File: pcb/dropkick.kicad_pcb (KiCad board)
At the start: 2 copper layers, 44.5 x 50.8 mm, 51 parts, among them SW1 CONN3_020524_WRE, SW2 KMR211NG_LFS, U1 ATSAMD21G18A-AUT, U2 SAM-M8Q-0-10, U3 MCP73831T-2ACI/OT, U4 DPS310, U5 MPU-6050, U6 SPX3819-3.3, X1 microUSB, X2 JSTPH, X3 microsd, X5 32768Hz

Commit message: V2-SAM working draft
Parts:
- removed the C5 at (77.7, 85.9)
- removed JP2: 20021221-00010C4LF, lib_fr:3221-10-0300-00-TR
- removed JP4: HEADER-1X12, lib_fr:1X12_ROUND
- removed JP5: HEADER-1X16ROUND, lib_fr:1X16_ROUND
- removed R11: 4.7K, lib_fr:RESPACK_4X0603
- removed R14: 10K, lib_fr:0603-NO
- removed SJ4: SOLDERJUMPER, lib_fr:0603-NO
- removed TP1: TESTPOINTROUND1.5MM, lib_fr:TESTPOINT_ROUND_1.5MM
- removed X5: 32768Hz, lib_fr:XTAL3215
- added J1: Conn_01x08, Connector_PinHeader_2.54mm:PinHeader_1x09_P2.54mm_Vertical, F.Cu at (105.7, 55.0)
- added JP1: 3221-10-0300-00-TR, lib_fr:3221-10-0300-00-TR, B.Cu at (97.7, 55.7)
- added R4: 10K, Resistor_SMD:R_0603_1608Metric, F.Cu at (79.6, 57.7)
- added R5: 1K, Resistor_SMD:R_0603_1608Metric, F.Cu at (82.9, 50.2)
- added REF2: OSHW-Logo2_7.3x6mm_SilkScreen, Symbol:OSHW-Logo2_7.3x6mm_SilkScreen, F.Cu at (70.5, 86.7)
- added X4: 32768Hz, lib_fr:XTAL3215, F.Cu at (83.7, 61.6)
- C1: footprint lib_fr:0603-NO -> Capacitor_SMD:C_0603_1608Metric
- C10: renamed from C11; value 10uF -> 0.1uF; footprint lib_fr:0805-NO -> Capacitor_SMD:C_0603_1608Metric
- C2, C3, C4: footprint lib_fr:0805-NO -> Capacitor_SMD:C_0805_2012Metric
- C5: renamed from C6; value 0.1uF -> 10uF; footprint lib_fr:0603-NO -> Capacitor_SMD:C_0805_2012Metric
- C6: renamed from C7; footprint lib_fr:0603-NO -> Capacitor_SMD:C_0603_1608Metric
- C7: renamed from C8; footprint lib_fr:0603-NO -> Capacitor_SMD:C_0603_1608Metric
- C8: renamed from C9; footprint lib_fr:0805-NO -> Capacitor_SMD:C_0805_2012Metric
- C9: renamed from C10; footprint lib_fr:0603-NO -> Capacitor_SMD:C_0603_1608Metric
- CHG1, L1, L2: footprint lib_fr:CHIPLED_0805_NOOUTLINE -> lib_fr:CHIPLED_0603_NOOUTLINE
- D1: moved to B.Cu
- R10, R7: footprint lib_fr:0603-NO -> Resistor_SMD:R_0603_1608Metric
- R2: value 100K -> 100k
- R3: value 100k -> 100K
- R6: value 10K -> 2.2K; footprint lib_fr:0603-NO -> Resistor_SMD:R_0603_1608Metric
- R8: value 2.2K -> 10K; footprint lib_fr:0603-NO -> Resistor_SMD:R_0603_1608Metric
- R9: value 1K -> 10K; footprint lib_fr:0603-NO -> Resistor_SMD:R_0603_1608Metric
- SW1: value CONN3_020524_WRE -> 450405020524
- U1: value ATSAMD21G18A-AUT -> SPX3819-3.3; footprint lib_fr:ATSAMD21G15B-AU -> lib_fr:SOT23-5
- U4: value DPS310 -> ATSAMD21G18A-AUT; footprint lib_fr:DPS310XTSA1 -> lib_fr:ATSAMD21G15B-AU
- U5: value MPU-6050 -> DPS310XTSA1; footprint lib_fr:QFN24_4MM_SMSC -> lib_fr:DPS310XTSA1
- U6: value SPX3819-3.3 -> MPU-6050; footprint lib_fr:SOT23-5 -> lib_fr:QFN24_4MM_SMSC
- moved D2 46.0 mm to (74.2, 45.7), turned to -90 degrees
- moved R10 43.2 mm to (102.9, 58.8), turned to -90 degrees
- moved C10 30.2 mm to (96.9, 66.3), turned to -90 degrees
- moved C12 27.1 mm to (101.7, 64.3), turned to 90 degrees
- moved R8 27.0 mm to (72.6, 48.2), turned to 0 degrees
- moved C11 26.1 mm to (101.4, 72.8), turned to 0 degrees
- moved D1 24.7 mm to (79.3, 50.5), turned to 180 degrees
- moved C5 24.5 mm to (75.5, 84.0), turned to 180 degrees
- moved R3 24.4 mm to (82.5, 69.4), turned to -90 degrees
- moved R9 24.2 mm to (101.0, 58.8)
- moved C2 23.1 mm to (85.6, 54.8)
- moved U5 22.9 mm to (99.2, 63.0)
- moved U4 20.0 mm to (90.2, 65.3), turned to 0 degrees
- moved R2 18.8 mm to (94.6, 53.5)
- moved R6 16.3 mm to (98.7, 46.9)
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- renumbered C12 to C11, C13 to C12, REF** to REF1
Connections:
- C10 pad 1: 3.3V -> +3V3
- C5 pad 1: 3.3V -> +3V3
- C6 pad 1: Net-(C7-Pad1) -> Net-(C6-Pad1)
- C7 pad 1: Net-(C8-Pad1) -> Net-(C7-Pad1)
- C9 pad 1: Net-(C10-Pad1) -> Net-(C9-Pad1)
- R10 pad 1: 3.3V -> +3V3
- R10 pad 2: Net-(D2-PadA) -> /SDA
- R2 pad 1: /D9 -> VBUS
- R2 pad 2: GND -> /EN
- R3 pad 1: VBUS -> /D9
- R3 pad 2: /EN -> GND
- R6 pad 1: Net-(R6-Pad1) -> /D13
- R6 pad 2: GND -> Net-(L2-PadA)
- R7 pad 1: Net-(CHG1-PadC) -> Net-(L1-PadC)
- R7 pad 2: Net-(R7-Pad2) -> GND
- R8 pad 1: /D13 -> +3V3
- R8 pad 2: Net-(L2-PadA) -> Net-(D2-PadA)
- R9 pad 1: Net-(L1-PadC) -> +3V3
- R9 pad 2: GND -> /SCL
- U1 pad 1: Net-(C7-Pad1) -> VBUS
- U1 pad 2: Net-(C8-Pad1) -> GND
- U1 pad 3: /A0 -> /EN
- U1 pad 4: /AREF -> unconnected-(U1-Pad4)
- U1 pad 5: GND -> +3V3
- U2 pad 17: 3.3V -> +3V3
- U2 pad 2: 3.3V -> +3V3
- U3 pad 1: Net-(R7-Pad2) -> Net-(R5-Pad2)
- U3 pad 5: Net-(R6-Pad1) -> Net-(R4-Pad1)
- U4 pad 1: GND -> Net-(C6-Pad1)
- U4 pad 2: GND -> Net-(C7-Pad1)
- U4 pad 3: /SDA -> /A0
- U4 pad 4: /SCL -> /AREF
- U4 pad 6: 3.3V -> +3V3
- U4 pad 7: GND -> /A1
- U4 pad 8: 3.3V -> /A2
- U5 pad 2: (no net) -> GND
- U5 pad 3: (no net) -> /SDA
- U5 pad 4: (no net) -> /SCL
- U5 pad 5: (no net) -> GND
- U5 pad 6: /SDA_EXT -> +3V3
- U5 pad 7: /SCL_EXT -> GND
- U5 pad 8: 3.3V -> +3V3
- U6 pad 1: VBUS -> GND
- U6 pad 2: GND -> (no net)
- U6 pad 3: /EN -> (no net)
- U6 pad 4: unconnected-(U6-Pad4) -> (no net)
- U6 pad 5: +3V3 -> (no net)
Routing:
- net GND: track 337.6 -> 75.3 mm, vias 1 -> 18
- net 3.3V: track 116.2 -> 0.00 mm, vias 3 -> 0
- net +3V3: track 118.3 -> 230.0 mm
- net /SCL: track 109.6 -> 40.3 mm, vias 2 -> 3
- net /SDA: track 105.4 -> 51.7 mm
- net VCC: track 37.4 -> 0.00 mm, vias 1 -> 0
- net /D8: track 58.3 -> 27.0 mm, vias 6 -> 0
- net /A5: track 30.9 -> 0.00 mm, vias 1 -> 0
- net /MOSI: track 55.6 -> 26.0 mm
- net /D7: track 50.3 -> 22.0 mm
- net /~{RESET}: track 46.6 -> 18.6 mm, vias 1 -> 0
- net VBUS: track 65.1 -> 37.1 mm, vias 2 -> 3
- net /A1: track 25.4 -> 0.00 mm
- net /A2: track 24.5 -> 0.00 mm
- net /A4: track 24.0 -> 0.00 mm
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- added copper zone on In1.Cu, net GND
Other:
- outline, holes or cut-outs redrawn
- copper layers 2 -> 4
- board text added: "+3.3"
- board text added: "A0"
- board text added: "AREF"
- board text added: "D0"
- board text added: "D1"
- board text added: "Dropkick V2-SAM Copyright (c) 2022 Riley Rainey https://GitHub.com/rrainey/dropkick/"
- board text added: "Dropkick V2-SAM Riley Rainey"
- board text added: "GND"
- board text added: "SCL"
- board text added: "SDA"
- board text added: "VBAT"
- board text removed: "Dropkick V1 Copyright (c) 2022 Riley Rainey https://GitHub.com/rrainey/dropkick/"

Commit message: test of 4-layer PCB
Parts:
- D1: moved to F.Cu
- moved C3 16.8 mm to (80.0, 54.2)
- moved C8 8.26 mm to (73.0, 54.4), turned to 90 degrees
- moved R5 7.65 mm to (75.3, 50.6), turned to -90 degrees
- moved D1 7.48 mm to (77.3, 57.7)
- moved R4 6.56 mm to (78.0, 51.3)
- moved U3 4.22 mm to (76.6, 54.1), turned to -90 degrees
- moved C4 2.04 mm to (97.5, 55.9)
- moved U1 2.04 mm to (93.8, 54.3)
- moved R2 2.04 mm to (96.6, 53.1)
- moved C2 0.95 mm to (86.5, 54.7), turned to 90 degrees
- moved R8 0.70 mm to (72.6, 47.5)
- moved C10 0.69 mm to (97.5, 66.7)
- moved C12 0.19 mm to (101.9, 64.3)
- moved C11 0.19 mm to (101.6, 72.7)
- moved U5 0.19 mm to (99.4, 63.0)
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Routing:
- net +3V3: track 230.0 -> 190.2 mm, vias 6 -> 5
- net /D+: track 44.3 -> 17.1 mm, vias 2 -> 0
- net /D-: track 38.1 -> 17.8 mm
- net /D13: track 35.1 -> 22.3 mm, vias 2 -> 0
- net /SCK: track 31.7 -> 22.8 mm, vias 2 -> 1
- net /SCL: track 40.3 -> 47.9 mm
- net VBUS: track 37.1 -> 30.2 mm, vias 3 -> 2
- net GND: track 75.3 -> 68.4 mm, vias 18 -> 15
- net /SDA: track 51.7 -> 45.8 mm, vias 4 -> 3
- net Net-(CHG1-PadC): track 5.25 -> 10.1 mm
- net /D8: track 27.0 -> 22.8 mm, vias 0 -> 2
- net Net-(R5-Pad2): track 7.11 -> 3.03 mm
- net /MISO: track 27.9 -> 24.5 mm
- net /SWDIO: track 13.3 -> 10.3 mm
- net /A0: track 23.6 -> 20.7 mm
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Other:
- board text added: "OFF ON"

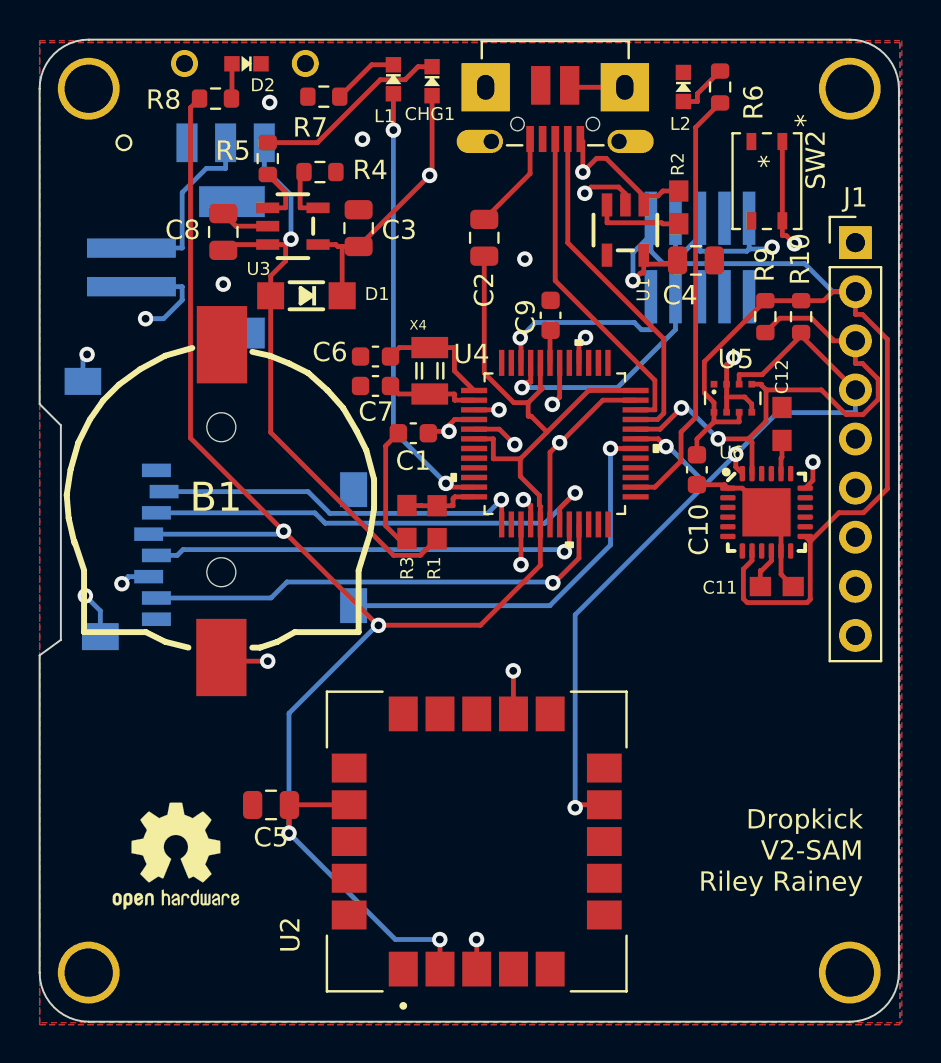
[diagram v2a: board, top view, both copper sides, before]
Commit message: V2-SAM PCB; now back to 2 layers
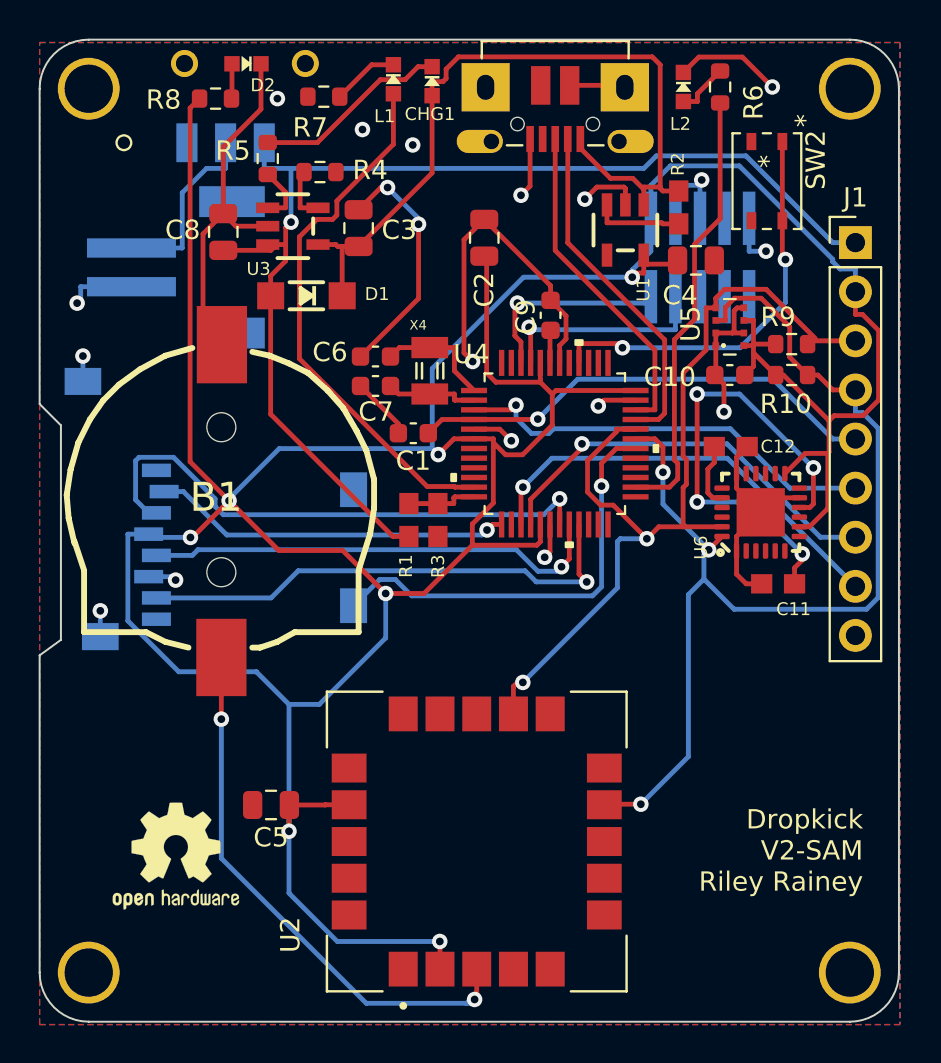
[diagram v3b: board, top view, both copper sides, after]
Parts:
- moved C10 5.19 mm to (99.2, 61.8), turned to 180 degrees
- moved U5 3.70 mm to (99.2, 59.3), turned to 90 degrees
- moved R10 3.06 mm to (102.4, 61.8), turned to 0 degrees
- moved C12 2.90 mm to (99.2, 65.5), turned to 0 degrees
- moved R9 1.97 mm to (102.4, 60.2), turned to 0 degrees
- moved R3 1.60 mm to (84.1, 69.3)
- moved R1 1.46 mm to (82.6, 69.3)
- moved U6 0.30 mm to (100.8, 68.9), turned to 90 degrees
- moved C11 0.16 mm to (101.7, 72.6), turned to 180 degrees
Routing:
- net GND: track 68.4 -> 104.5 mm, vias 15 -> 19
- net /REGOUT: track 2.12 -> 24.1 mm, vias 0 -> 4
- net +3V3: track 190.2 -> 205.2 mm, vias 5 -> 7
- net /SDA: track 45.8 -> 57.7 mm
- net VBUS: track 30.2 -> 40.9 mm, vias 2 -> 0
- net /VBACKUP: track 22.6 -> 29.2 mm
- net /D8: track 22.8 -> 28.0 mm, vias 2 -> 0
- net /MOSI: track 24.5 -> 28.1 mm
- net /D1: track 19.8 -> 22.5 mm
- net /D0: track 19.5 -> 21.4 mm
- net /MISO: track 24.5 -> 26.2 mm
- net /CPOUT: track 1.74 -> 3.37 mm
- net /D7: track 20.9 -> 22.4 mm
- net /A0: track 20.7 -> 22.2 mm
- net /AREF: track 25.9 -> 24.5 mm
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- removed copper zone on In1.Cu, net GND
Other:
- copper layers 4 -> 2
- board text added: "{dblquote}OFF{dblquote} {dblquote}ON{dblquote}"
- board text removed: "OFF ON"
